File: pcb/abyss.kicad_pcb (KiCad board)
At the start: 2 copper layers, 109.1 x 96.1 mm, 34 parts

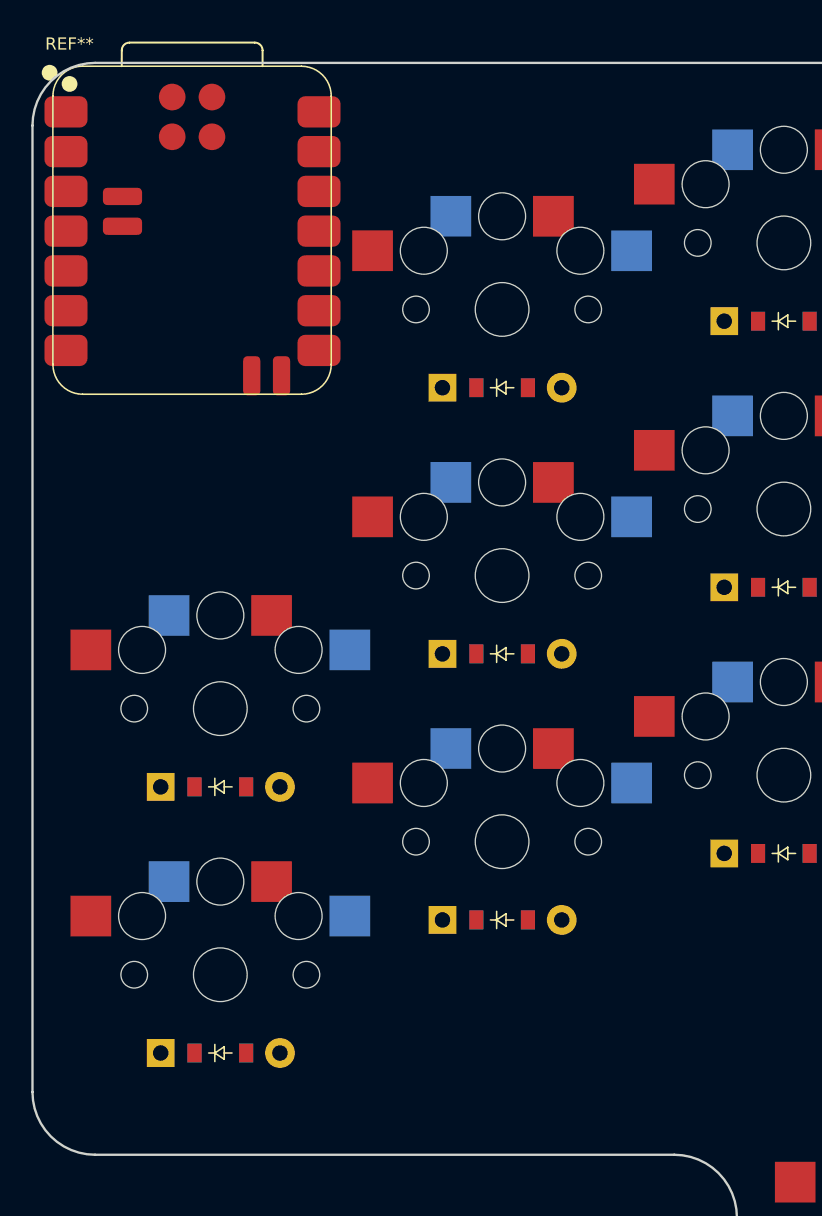
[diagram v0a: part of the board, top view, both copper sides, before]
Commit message: Add power switch footprint
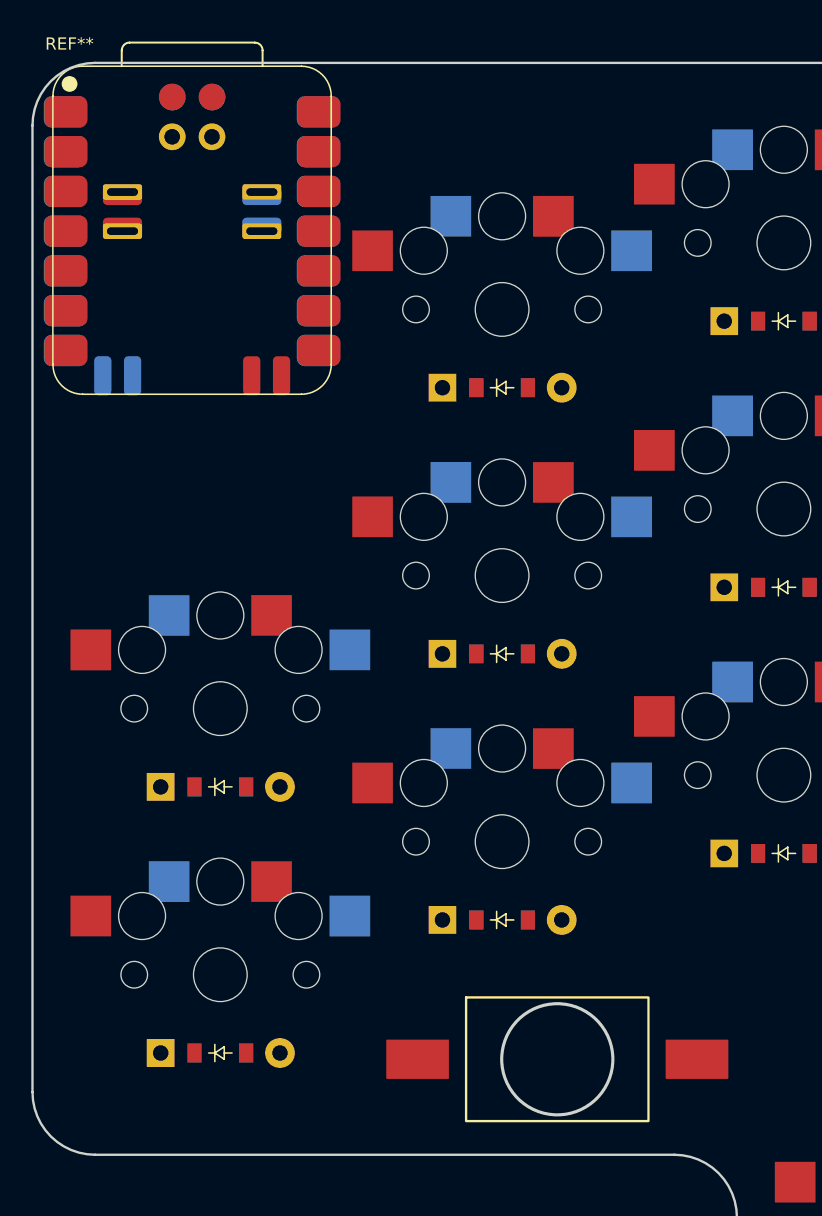
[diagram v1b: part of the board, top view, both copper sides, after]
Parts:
- added REF**: 1208YD, footprints:1208YD, F.Cu at (121.5, 105.4)

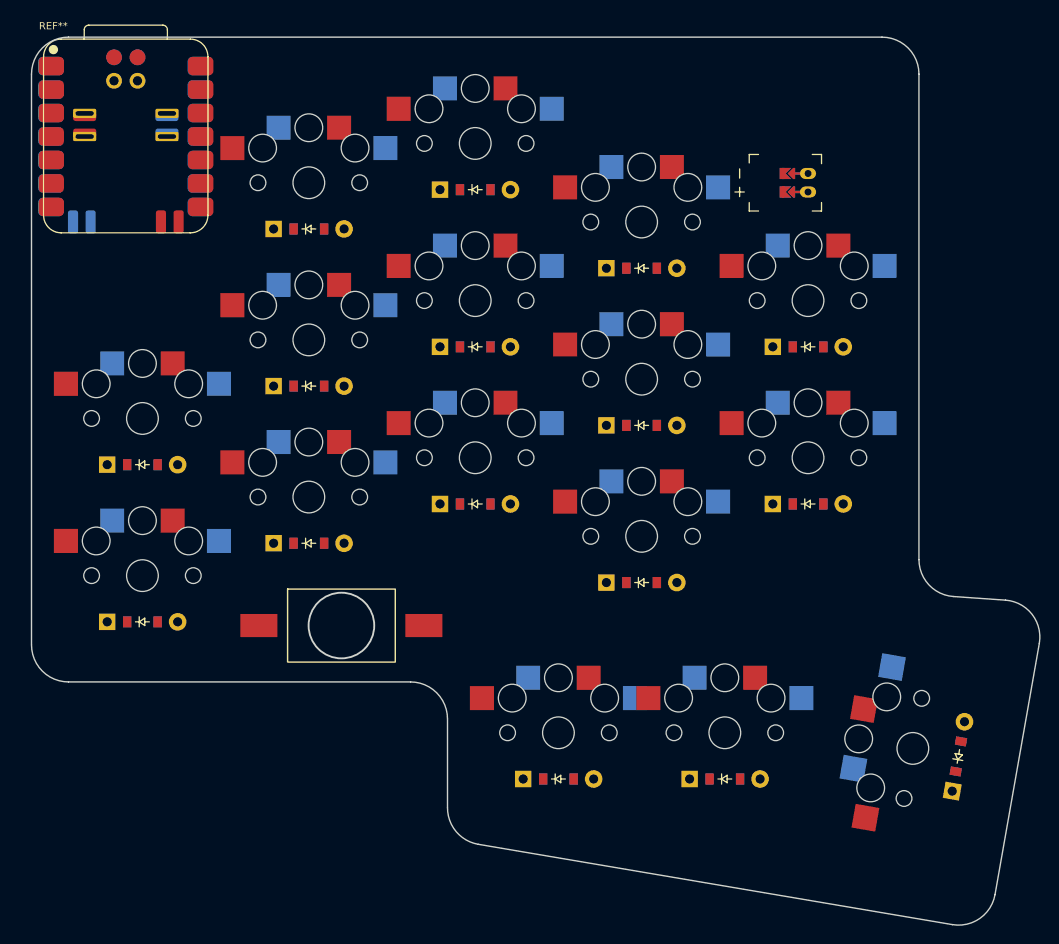
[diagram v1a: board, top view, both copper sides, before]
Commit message: Fix tolerences
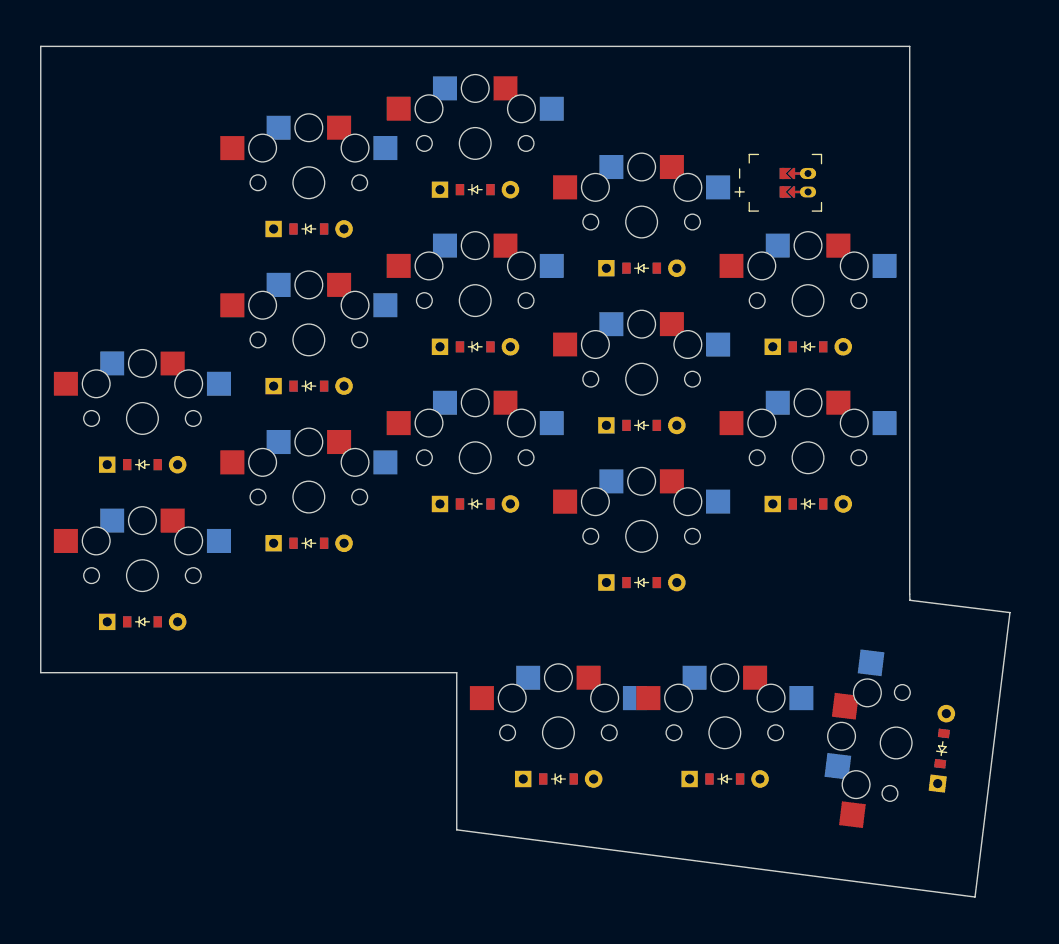
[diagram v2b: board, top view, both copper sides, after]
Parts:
- removed REF**: 1208YD, footprints:1208YD
- removed REF**: XIAO-nRF52840-SMD, footprints:XIAO-nRF52840-SMD
- moved D16 1.96 mm to (186.5, 118.7), turned to 83 degrees
- moved S16 1.90 mm to (181.5, 118.1), turned to 83 degrees
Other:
- board size 109.1 x 96.1 mm -> 104.8 x 92 mm

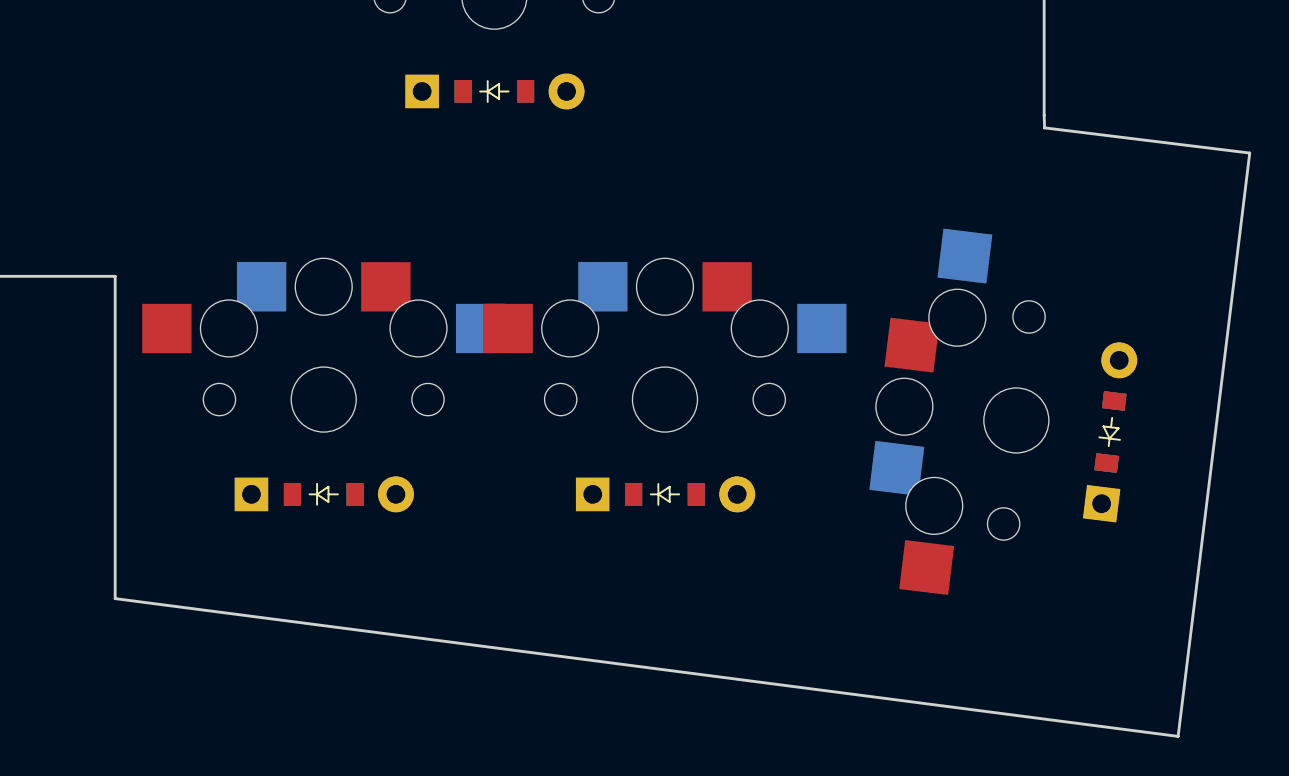
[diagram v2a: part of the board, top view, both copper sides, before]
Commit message: Fix pcb size
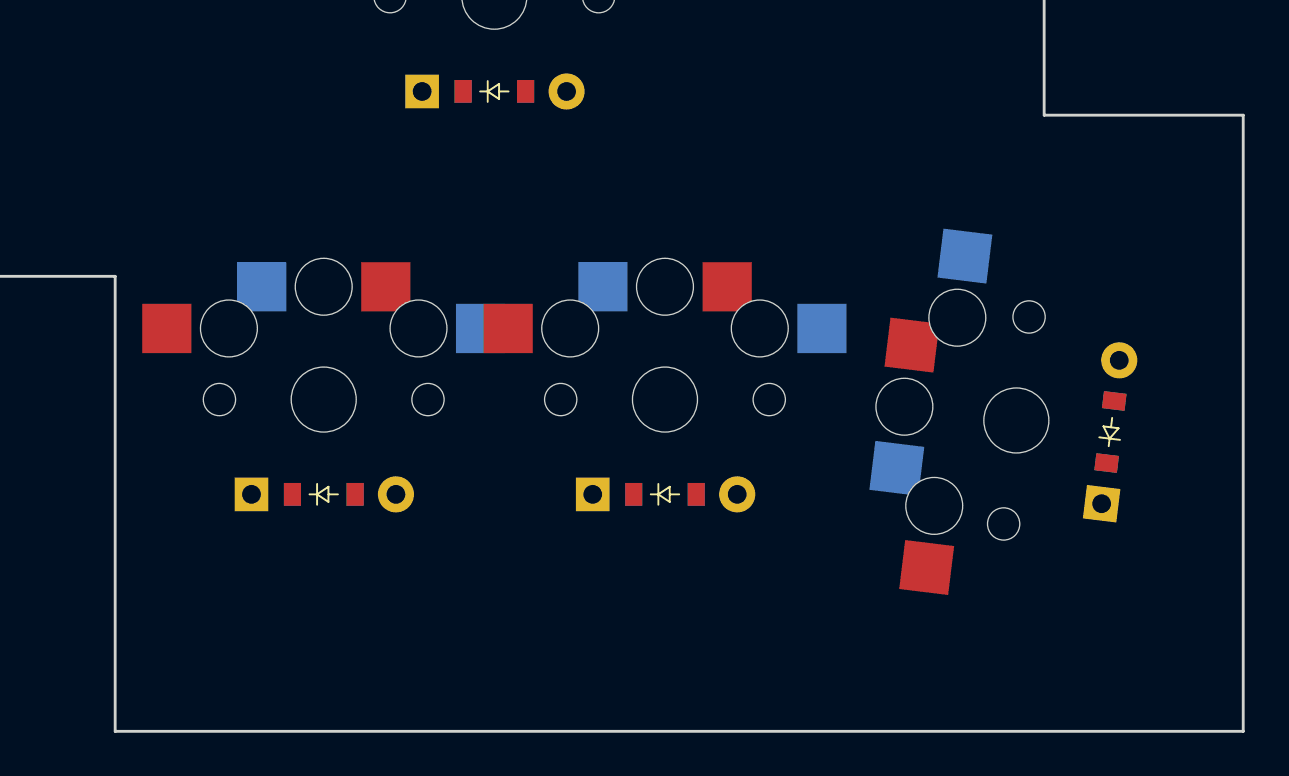
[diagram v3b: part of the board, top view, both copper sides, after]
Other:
- board size 104.8 x 92 mm -> 104.5 x 91.8 mm
- net class Default added: clearance 0.2, trace_width 0.25, via_dia 0.8, via_drill 0.4

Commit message: Reinit pcb
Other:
- net class Default removed

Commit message: wip: Pcb
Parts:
- added REF**: XIAO Pin, Library:seeed-xiao-nRF54L15, F.Cu at (97.0, 53.5)

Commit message: Fix angles
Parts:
- moved REF** 0.52 mm to (97.5, 53.4)
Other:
- board size 104.5 x 91.8 mm -> 106.5 x 91.8 mm
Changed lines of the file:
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@@
 	(footprint "Library:seeed-xiao-nRF54L15"
 		(layer "F.Cu")
-		(at 97 53.5 90)
+		(at 97.5 53.37 90)
 		(property "Reference" "REF**"
 			(at 0.0523 -10.696 90)
@@
 	(gr_line
 		(start 193.5 134.5)
-		(end 134 134.5)
+		(end 156.5 134.5)
+		(stroke
+			(width 0.15)
+			(type solid)
+		)
+		(layer "Edge.Cuts")
+	)
+	(gr_line
+		(start 187 102)
+		(end 187 105.25)
+		(stroke
+			(width 0.15)
+			(type solid)
+		)
+		(layer "Edge.Cuts")
+	)
+	(gr_line
+		(start 150 131.25)
+		(end 150 134.5)
 		(stroke
 			(width 0.15)
@@
 	)
 	(gr_line
-		(start 193.5 102)
+		(start 117.25 46)
+		(end 117.25 42.75)
+		(stroke
+			(width 0.15)
+			(type solid)
+		)
+		(layer "Edge.Cuts")
+	)
+	(gr_line
+		(start 117.25 42.75)
+		(end 87 42.75)
+		(stroke
+			(width 0.15)
+			(type solid)
+		)
+		(layer "Edge.Cuts")
+	)
+	(gr_line
+		(start 193.5 105.25)
 		(end 193.5 134.5)
 		(stroke
@@
 	)
 	(gr_line
-		(start 89 110.5)
-		(end 89 42.75)
+		(start 87 110.5)
+		(end 87 42.75)
+		(stroke
+			(width 0.15)
+			(type solid)
+		)
+		(layer "Edge.Cuts")
+	)
+	(gr_line
+		(start 187 105.25)
+		(end 193.5 105.25)
 		(stroke
 			(width 0.15)
@@
 	)
 	(gr_line
-		(start 89 42.75)
+		(start 123.25 107.25)
+		(end 123.25 110.5)
+		(stroke
+			(width 0.15)
+			(type solid)
+		)
+		(layer "Edge.Cuts")
+	)
+	(gr_line
+		(start 150 134.5)
+		(end 134 134.5)
+		(stroke
+			(width 0.15)
+			(type solid)
+		)
+		(layer "Edge.Cuts")
+	)
+	(gr_line
+		(start 123.75 42.75)
 		(end 183 42.75)
 		(stroke
@@
 	)
 	(gr_line
+		(start 116.75 110.5)
+		(end 116.75 107.25)
+		(stroke
+			(width 0.15)
+			(type solid)
+		)
+		(layer "Edge.Cuts")
+	)
+	(gr_line
 		(start 183 42.75)
 		(end 183 102)
@@
 	)
 	(gr_line
-		(start 134 110.5)
-		(end 89 110.5)
+		(start 116.75 110.5)
+		(end 87 110.5)
+		(stroke
+			(width 0.15)
+			(type solid)
+		)
+		(layer "Edge.Cuts")
+	)
+	(gr_line
+		(start 116.75 107.25)
+		(end 123.25 107.25)
+		(stroke
+			(width 0.15)
+			(type solid)
+		)
+		(layer "Edge.Cuts")
+	)
+	(gr_line
+		(start 156.5 134.5)
+		(end 156.5 131.25)
+		(stroke
+			(width 0.15)
+			(type solid)
+		)
+		(layer "Edge.Cuts")
+	)
+	(gr_line
+		(start 123.75 42.75)
+		(end 123.75 46)
+		(stroke
+			(width 0.15)
+			(type solid)
+		)
+		(layer "Edge.Cuts")
+	)
+	(gr_line
+		(start 123.25 110.5)
+		(end 134 110.5)
+		(stroke
+			(width 0.15)
+			(type solid)
+		)
+		(layer "Edge.Cuts")
+	)
+	(gr_line
+		(start 156.5 131.25)
+		(end 150 131.25)
 		(stroke
 			(width 0.15)
@@
 	(gr_line
 		(start 183 102)
-		(end 193.5 102)
+		(end 187 102)
+		(stroke
+			(width 0.15)
+			(type solid)
+		)
+		(layer "Edge.Cuts")
+	)
+	(gr_line
+		(start 123.75 46)
+		(end 117.25 46)
 		(stroke
 			(width 0.15)

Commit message: Add reset button to pcb
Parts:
- added REF**: ResetBtn, Library:ResetBtn, F.Cu at (166.4, 102.6)
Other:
- board size 106.5 x 91.8 mm -> 106.6 x 91.8 mm
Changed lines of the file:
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@@
 		(embedded_fonts no)
 	)
+	(footprint "Library:ResetBtn"
+		(layer "F.Cu")
+		(at 166.4 102.6)
+		(property "Reference" "REF**"
+			(at 0 -0.5 0)
+			(unlocked yes)
+			(layer "F.SilkS")
+			(hide yes)
+			(effects
+				(font
+					(size 1 1)
+					(thickness 0.1)
+				)
+			)
+		)
+		(property "Value" "ResetBtn"
+			(at 0 1 0)
+			(unlocked yes)
+			(layer "F.Fab")
+			(hide yes)
+			(effects
+				(font
+					(size 1 1)
+					(thickness 0.15)
+				)
+			)
+		)
+		(property "Datasheet" ""
+			(at 0 0 0)
+			(unlocked yes)
+			(layer "F.Fab")
+			(hide yes)
+			(effects
+				(font
+					(size 1 1)
+					(thickness 0.15)
+				)
+			)
+		)
+		(property "Description" ""
+			(at 0 0 0)
+			(unlocked yes)
+			(layer "F.Fab")
+			(hide yes)
+			(effects
+				(font
+					(size 1 1)
+					(thickness 0.15)
+				)
+			)
+		)
+		(attr smd)
+		(fp_line
+			(start -3.5 1.5)
+			(end -3.5 -1.5)
+			(stroke
+				(width 0.2)
+				(type default)
+			)
+			(layer "F.Cu")
+		)
+		(fp_line
+			(start 3.5 1.5)
+			(end 3.5 -1.5)
+			(stroke
+				(width 0.2)
+				(type default)
+			)
+			(layer "F.Cu")
+		)
+		(fp_line
+			(start -3.5 -1.5)
+			(end -3.5 2)
+			(stroke
+				(width 0.2)
+				(type default)
+			)
+			(layer "B.Cu")
+		)
+		(fp_line
+			(start 3.5 2)
+			(end 3.5 -1.5)
+			(stroke
+				(width 0.2)
+				(type default)
+			)
+			(layer "B.Cu")
+		)
+		(fp_rect
+			(start -3 -3)
+			(end 3 3)
+			(stroke
+				(width 0.1)
+				(type default)
+			)
+			(fill no)
+			(layer "F.SilkS")
+		)
+		(fp_rect
+			(start -3 -3)
+			(end 3 3)
+			(stroke
+				(width 0.1)
+				(type default)
+			)
+			(fill no)
+			(layer "B.SilkS")
+		)
+		(fp_circle
+			(center 0 0)
+			(end 2 -1.5)
+			(stroke
+				(width 0.05)
+				(type default)
+			)
+			(fill no)
+			(layer "Edge.Cuts")
+		)
+		(pad "1" smd roundrect
+			(at -3 -3)
+			(size 3 3)
+			(layers "F.Cu" "F.Mask" "F.Paste")
+			(roundrect_rratio 0.15)
+			(thermal_bridge_angle 45)
+		)
+		(pad "1" smd roundrect
+			(at -3 -3)
+			(size 3 3)
+			(layers "B.Cu" "B.Mask" "B.Paste")
+			(roundrect_rratio 0.15)
+			(thermal_bridge_angle 45)
+		)
+		(pad "1" smd roundrect
+			(at -3 3)
+			(size 3 3)
+			(layers "F.Cu" "F.Mask" "F.Paste")
+			(roundrect_rratio 0.15)
+			(thermal_bridge_angle 45)
+		)
+		(pad "1" smd roundrect
+			(at -3 3)
+			(size 3 3)
+			(layers "B.Cu" "B.Mask" "B.Paste")
+			(roundrect_rratio 0.15)
+			(thermal_bridge_angle 45)
+		)
+		(pad "1" smd roundrect
+			(at 3 -3)
+			(size 3 3)
+			(layers "F.Cu" "F.Mask" "F.Paste")
+			(roundrect_rratio 0.15)
+			(thermal_bridge_angle 45)
+		)
+		(pad "1" smd roundrect
+			(at 3 -3)
+			(size 3 3)
+			(layers "B.Cu" "B.Mask" "B.Paste")
+			(roundrect_rratio 0.15)
+			(thermal_bridge_angle 45)
+		)
+		(pad "1" smd roundrect
+			(at 3 3)
+			(size 3 3)
+			(layers "F.Cu" "F.Mask" "F.Paste")
+			(roundrect_rratio 0.15)
+			(thermal_bridge_angle 45)
+		)
+		(pad "1" smd roundrect
+			(at 3 3)
+			(size 3 3)
+			(layers "B.Cu" "B.Mask" "B.Paste")
+			(roundrect_rratio 0.15)
+			(thermal_bridge_angle 45)
+		)
+		(embedded_fonts no)
+	)
 	(footprint "PG1350"
 		(layer "F.Cu")
@@
 	(gr_line
 		(start 193.5 134.5)
-		(end 156.5 134.5)
+		(end 167.9 134.5)
 		(stroke
 			(width 0.15)
@@
 	)
 	(gr_line
-		(start 150 131.25)
-		(end 150 134.5)
+		(start 161.4 131.25)
+		(end 161.4 134.5)
 		(stroke
 			(width 0.15)
@@
 	)
 	(gr_line
-		(start 117.25 46)
-		(end 117.25 42.75)
+		(start 109 46)
+		(end 109 42.75)
 		(stroke
 			(width 0.15)
@@
 	)
 	(gr_line
-		(start 117.25 42.75)
-		(end 87 42.75)
+		(start 109 42.75)
+		(end 86.9 42.75)
 		(stroke
 			(width 0.15)
@@
 	)
 	(gr_line
-		(start 123.25 107.25)
-		(end 123.25 110.5)
+		(start 115.6 107.25)
+		(end 115.6 110.5)
 		(stroke
 			(width 0.15)
@@
 	)
 	(gr_line
-		(start 150 134.5)
+		(start 161.4 134.5)
 		(end 134 134.5)
 		(stroke
@@
 	)
 	(gr_line
-		(start 123.75 42.75)
+		(start 115.5 42.75)
 		(end 183 42.75)
 		(stroke
@@
 	)
 	(gr_line
-		(start 116.75 110.5)
-		(end 116.75 107.25)
+		(start 109.1 110.5)
+		(end 109.1 107.25)
 		(stroke
 			(width 0.15)
@@
 	)
 	(gr_line
-		(start 116.75 110.5)
+		(start 109.1 110.5)
 		(end 87 110.5)
 		(stroke
@@
 	)
 	(gr_line
-		(start 116.75 107.25)
-		(end 123.25 107.25)
+		(start 109.1 107.25)
+		(end 115.6 107.25)
 		(stroke
 			(width 0.15)
@@
 	)
 	(gr_line
-		(start 156.5 134.5)
-		(end 156.5 131.25)
+		(start 167.9 134.5)
+		(end 167.9 131.25)
 		(stroke
 			(width 0.15)
@@
 	)
 	(gr_line
-		(start 123.75 42.75)
-		(end 123.75 46)
+		(start 115.5 42.75)
+		(end 115.5 46)
 		(stroke
 			(width 0.15)
@@
 	)
 	(gr_line
-		(start 123.25 110.5)
+		(start 115.6 110.5)
 		(end 134 110.5)
 		(stroke
@@
 	)
 	(gr_line
-		(start 156.5 131.25)
-		(end 150 131.25)
+		(start 167.9 131.25)
+		(end 161.4 131.25)
 		(stroke
 			(width 0.15)
@@
 	)
 	(gr_line
-		(start 123.75 46)
-		(end 117.25 46)
+		(start 115.5 46)
+		(end 109 46)
 		(stroke
 			(width 0.15)
